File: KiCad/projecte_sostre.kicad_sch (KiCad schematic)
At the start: 0 parts

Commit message: esquematic modificat
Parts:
- added U1: CDCV304, Package_SO:TSSOP-8_4.4x3mm_P0.65mm, symbol Buffer:CDCV304
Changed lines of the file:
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@@
 	(generator_version "9.0")
 	(paper "A4")
+	(symbol
+		(lib_id "Buffer:CDCV304")
+		(at 62.23 67.31 0)
+		(unit 1)
+		(exclude_from_sim no)
+		(in_bom yes)
+		(on_board yes)
+		(dnp no)
+		(fields_autoplaced yes)
+		(property "Reference" "U1"
+			(at 64.3733 54.61 0)
+			(effects
+				(font
+					(size 1.27 1.27)
+				)
+				(justify left)
+			)
+		)
+		(property "Value" "CDCV304"
+			(at 64.3733 57.15 0)
+			(effects
+				(font
+					(size 1.27 1.27)
+				)
+				(justify left)
+			)
+		)
+		(property "Footprint" "Package_SO:TSSOP-8_4.4x3mm_P0.65mm"
+			(at 67.31 80.01 0)
+			(effects
+				(font
+					(size 1.27 1.27)
+				)
+				(justify left)
+				(hide yes)
+			)
+		)
+		(property "Datasheet" "https://www.ti.com/lit/ds/symlink/cdcv304.pdf"
+			(at 67.31 82.55 0)
+			(effects
+				(font
+					(size 1.27 1.27)
+				)
+				(justify left)
+				(hide yes)
+			)
+		)
+		(property "Description" "0-200 MHz 1:4 Clock Buffer, PCI-X Compliant, TSSOP-8"
+			(at 62.23 67.31 0)
+			(effects
+				(font
+					(size 1.27 1.27)
+				)
+				(hide yes)
+			)
+		)
+		(pin "3"
+		)
+		(pin "1"
+		)
+		(pin "2"
+		)
+		(pin "4"
+		)
+		(pin "8"
+		)
+		(pin "6"
+		)
+		(pin "5"
+		)
+		(pin "7"
+		)
+		(instances
+			(project ""
+				(path "/12dc51a9-2603-4518-b497-f55f3848c2a7"
+					(reference "U1")
+					(unit 1)
+				)
+			)
+		)
+	)
 	(sheet_instances
 		(path "/"

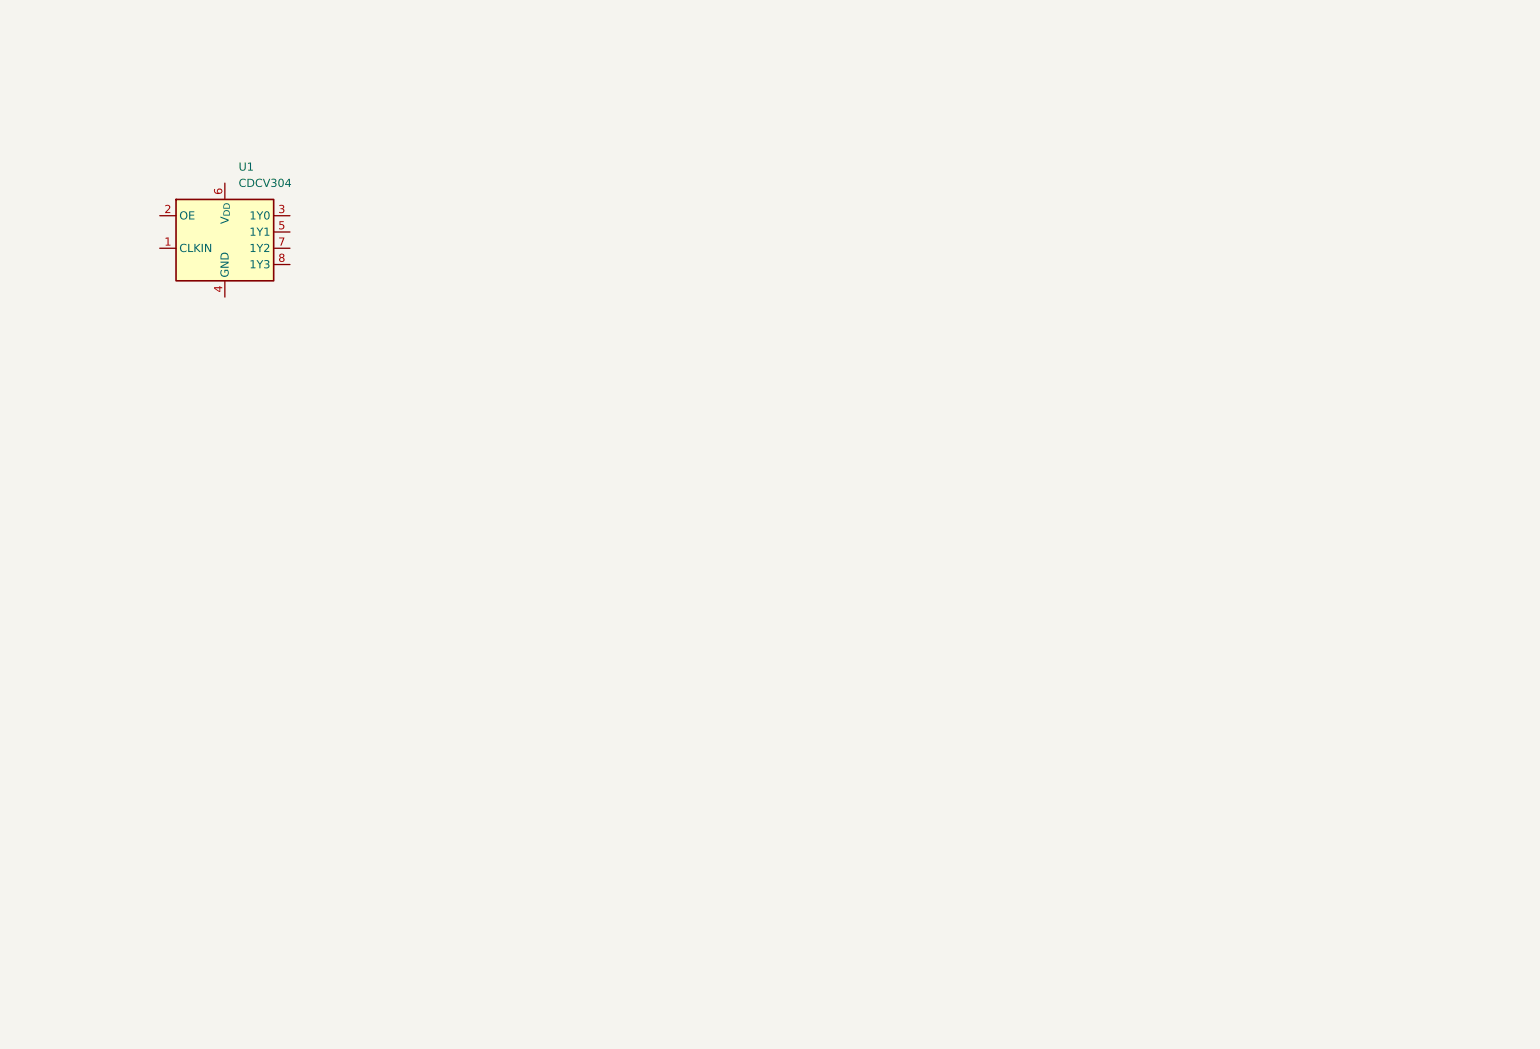
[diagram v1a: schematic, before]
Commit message: Començada part de micro i separacio de les 4 fases o grans grups de la PCB
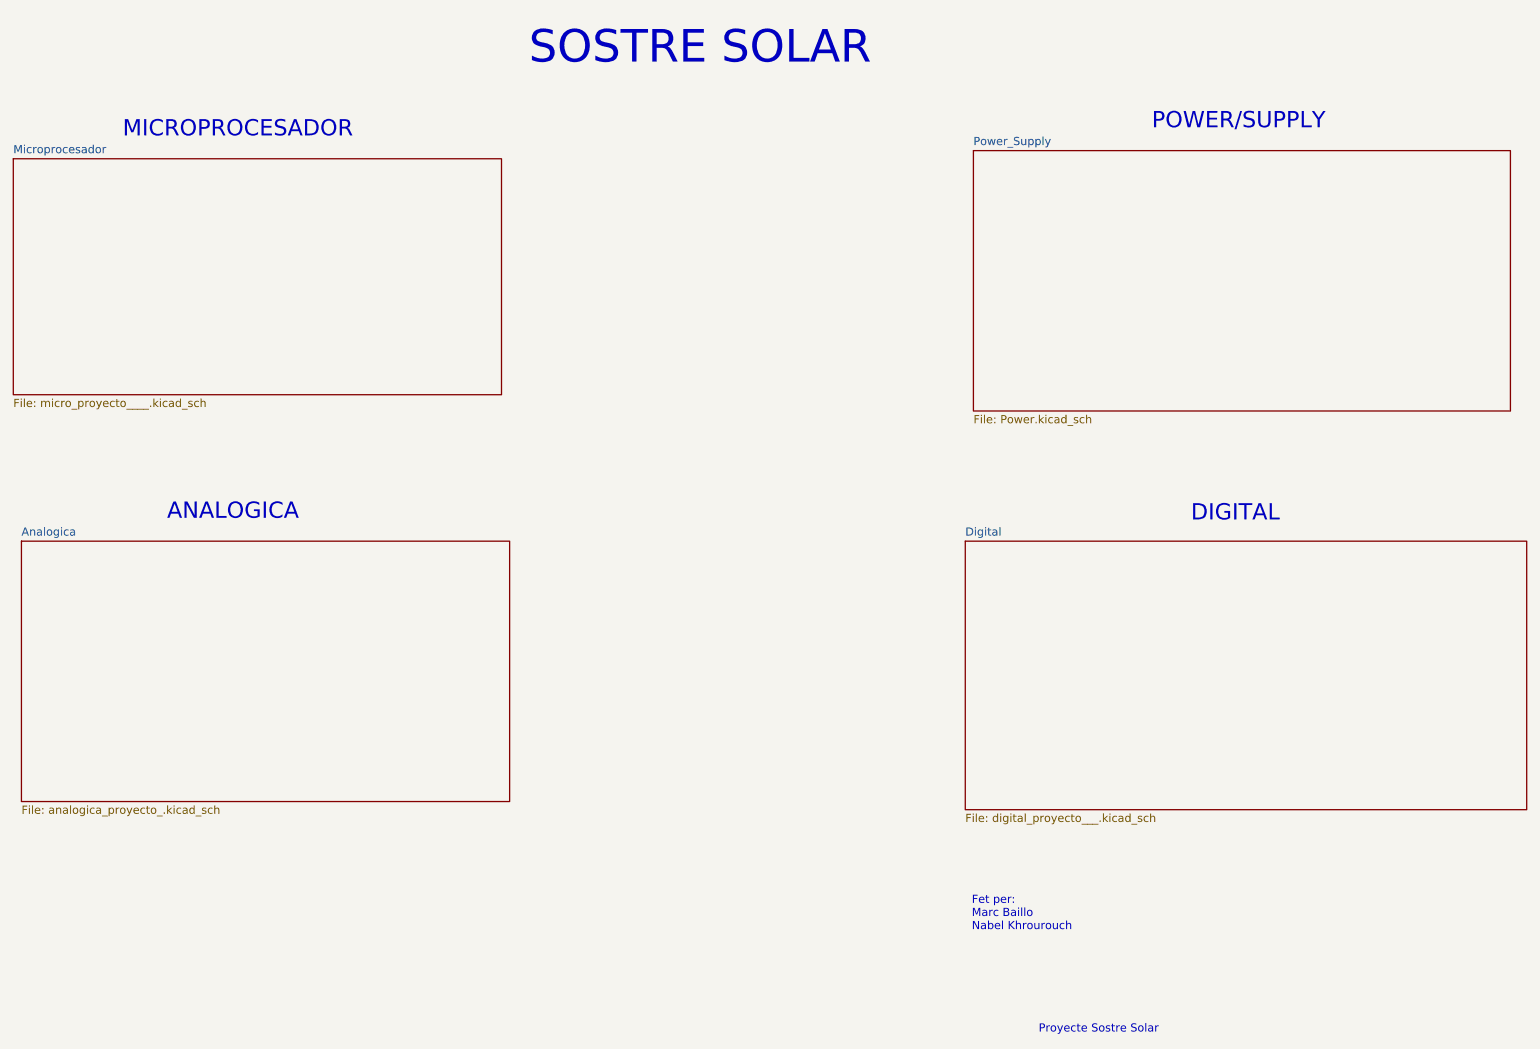
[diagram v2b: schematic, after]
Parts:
- removed U1: CDCV304, Package_SO:TSSOP-8_4.4x3mm_P0.65mm, symbol Buffer:CDCV304
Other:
- added sheet Analogica (analogica_proyecto_.kicad_sch)
- added sheet Digital (digital_proyecto___.kicad_sch)
- added sheet Microprocesador (micro_proyecto____.kicad_sch)
- added sheet Power_Supply (Power.kicad_sch)
- note added: "ANALOGICA"
- note added: "DIGITAL"
- note added: "Fet per: Marc Baillo Nabel Khrourouch"
- note added: "MICROPROCESADOR"
- note added: "POWER/SUPPLY"
- note added: "Proyecte Sostre Solar"
- note added: "SOSTRE SOLAR"
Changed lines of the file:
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@@
 	(generator_version "9.0")
 	(paper "A4")
-	(symbol
-		(lib_id "Buffer:CDCV304")
-		(at 62.23 67.31 0)
-		(unit 1)
-		(exclude_from_sim no)
-		(in_bom yes)
-		(on_board yes)
-		(dnp no)
-		(fields_autoplaced yes)
-		(property "Reference" "U1"
-			(at 64.3733 54.61 0)
-			(effects
-				(font
-					(size 1.27 1.27)
-				)
-				(justify left)
-			)
-		)
-		(property "Value" "CDCV304"
-			(at 64.3733 57.15 0)
-			(effects
-				(font
-					(size 1.27 1.27)
-				)
-				(justify left)
-			)
-		)
-		(property "Footprint" "Package_SO:TSSOP-8_4.4x3mm_P0.65mm"
-			(at 67.31 80.01 0)
-			(effects
-				(font
-					(size 1.27 1.27)
-				)
-				(justify left)
-				(hide yes)
-			)
-		)
-		(property "Datasheet" "https://www.ti.com/lit/ds/symlink/cdcv304.pdf"
-			(at 67.31 82.55 0)
-			(effects
-				(font
-					(size 1.27 1.27)
-				)
-				(justify left)
-				(hide yes)
-			)
-		)
-		(property "Description" "0-200 MHz 1:4 Clock Buffer, PCI-X Compliant, TSSOP-8"
-			(at 62.23 67.31 0)
-			(effects
-				(font
-					(size 1.27 1.27)
-				)
-				(hide yes)
-			)
-		)
-		(pin "3"
-		)
-		(pin "1"
-		)
-		(pin "2"
-		)
-		(pin "4"
-		)
-		(pin "8"
-		)
-		(pin "6"
-		)
-		(pin "5"
-		)
-		(pin "7"
-		)
-		(instances
-			(project ""
-				(path "/12dc51a9-2603-4518-b497-f55f3848c2a7"
-					(reference "U1")
-					(unit 1)
-				)
-			)
+	(text "SOSTRE SOLAR\n"
+		(exclude_from_sim no)
+		(at 136.398 36.068 0)
+		(effects
+			(font
+				(size 5.08 5.08)
+			)
+		)
+	)
+	(text "Proyecte Sostre Solar\n"
+		(exclude_from_sim no)
+		(at 198.628 189.23 0)
+		(effects
+			(font
+				(size 1.27 1.27)
+			)
+		)
+	)
+	(text "MICROPROCESADOR\n"
+		(exclude_from_sim no)
+		(at 64.262 48.768 0)
+		(effects
+			(font
+				(size 2.54 2.54)
+			)
+		)
+	)
+	(text "POWER/SUPPLY"
+		(exclude_from_sim no)
+		(at 220.472 47.498 0)
+		(effects
+			(font
+				(size 2.54 2.54)
+			)
+		)
+	)
+	(text "ANALOGICA\n"
+		(exclude_from_sim no)
+		(at 63.5 108.458 0)
+		(effects
+			(font
+				(size 2.54 2.54)
+			)
+		)
+	)
+	(text "Fet per:\nMarc Baillo\nNabel Khrourouch\n"
+		(exclude_from_sim no)
+		(at 178.816 171.196 0)
+		(effects
+			(font
+				(size 1.27 1.27)
+			)
+			(justify left)
+		)
+	)
+	(text "DIGITAL\n"
+		(exclude_from_sim no)
+		(at 219.964 108.712 0)
+		(effects
+			(font
+				(size 2.54 2.54)
+			)
+		)
+	)
+	(sheet
+		(at 179.07 52.07)
+		(size 83.82 40.64)
+		(exclude_from_sim no)
+		(in_bom yes)
+		(on_board yes)
+		(dnp no)
+		(fields_autoplaced yes)
+		(stroke
+			(width 0.1524)
+			(type solid)
+		)
+		(fill
+			(color 0 0 0 0.0000)
+		)
+		(property "Sheetname" "Power_Supply"
+			(at 179.07 51.3584 0)
+			(effects
+				(font
+					(size 1.27 1.27)
+				)
+				(justify left bottom)
+			)
+		)
+		(property "Sheetfile" "Power.kicad_sch"
+			(at 179.07 93.2946 0)
+			(effects
+				(font
+					(size 1.27 1.27)
+				)
+				(justify left top)
+			)
+		)
+		(instances
+			(project "projecte_sostre"
+				(path "/12dc51a9-2603-4518-b497-f55f3848c2a7"
+					(page "3")
+				)
+			)
+		)
+	)
+	(sheet
+		(at 177.8 113.03)
+		(size 87.63 41.91)
+		(exclude_from_sim no)
+		(in_bom yes)
+		(on_board yes)
+		(dnp no)
+		(fields_autoplaced yes)
+		(stroke
+			(width 0.1524)
+			(type solid)
+		)
+		(fill
+			(color 0 0 0 0.0000)
+		)
+		(property "Sheetname" "Digital"
+			(at 177.8 112.3184 0)
+			(effects
+				(font
+					(size 1.27 1.27)
+				)
+				(justify left bottom)
+			)
+		)
+		(property "Sheetfile" "digital_proyecto___.kicad_sch"
+			(at 177.8 155.5246 0)
+			(effects
+				(font
+					(size 1.27 1.27)
+				)
+				(justify left top)
+			)
+		)
+		(instances
+			(project "projecte_sostre"
+				(path "/12dc51a9-2603-4518-b497-f55f3848c2a7"
+					(page "5")
+				)
+			)
+		)
+	)
+	(sheet
+		(at 29.21 53.34)
+		(size 76.2 36.83)
+		(exclude_from_sim no)
+		(in_bom yes)
+		(on_board yes)
+		(dnp no)
+		(fields_autoplaced yes)
+		(stroke
+			(width 0.1524)
+			(type solid)
+		)
+		(fill
+			(color 0 0 0 0.0000)
+		)
+		(property "Sheetname" "Microprocesador"
+			(at 29.21 52.6284 0)
+			(effects
+				(font
+					(size 1.27 1.27)
+				)
+				(justify left bottom)
+			)
+		)
+		(property "Sheetfile" "micro_proyecto____.kicad_sch"
+			(at 29.21 90.7546 0)
+			(effects
+				(font
+					(size 1.27 1.27)
+				)
+				(justify left top)
+			)
+		)
+		(instances
+			(project "projecte_sostre"
+				(path "/12dc51a9-2603-4518-b497-f55f3848c2a7"
+					(page "2")
+				)
+			)
+		)
+	)
+	(sheet
+		(at 30.48 113.03)
+		(size 76.2 40.64)
+		(exclude_from_sim no)
+		(in_bom yes)
+		(on_board yes)
+		(dnp no)
+		(fields_autoplaced yes)
+		(stroke
+			(width 0.1524)
+			(type solid)
+		)
+		(fill
+			(color 0 0 0 0.0000)
+		)
+		(property "Sheetname" "Analogica"
+			(at 30.48 112.3184 0)
+			(effects
+				(font
+					(size 1.27 1.27)
+				)
+				(justify left bottom)
+			)
+		)
+		(property "Sheetfile" "analogica_proyecto_.kicad_sch"
+			(at 30.48 154.2546 0)
+			(effects
+				(font
+					(size 1.27 1.27)
+				)
+				(justify left top)
+			)
+		)
+		(instances
+			(project "projecte_sostre"
+				(path "/12dc51a9-2603-4518-b497-f55f3848c2a7"
+					(page "4")
+				)
+			)

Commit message: Prueba 1
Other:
- note added: "MICROCONTROLADOR"
- note removed: "MICROPROCESADOR"
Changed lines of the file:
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@@
 		)
 	)
-	(text "MICROPROCESADOR\n"
+	(text "MICROCONTROLADOR\n\n"
 		(exclude_from_sim no)
 		(at 64.262 48.768 0)
